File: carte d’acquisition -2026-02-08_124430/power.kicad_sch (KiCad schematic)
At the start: 19 parts, among them U1 MIC5365-3.3YC5, U4 TPS55285, U5 MIC5365-3.3YC5

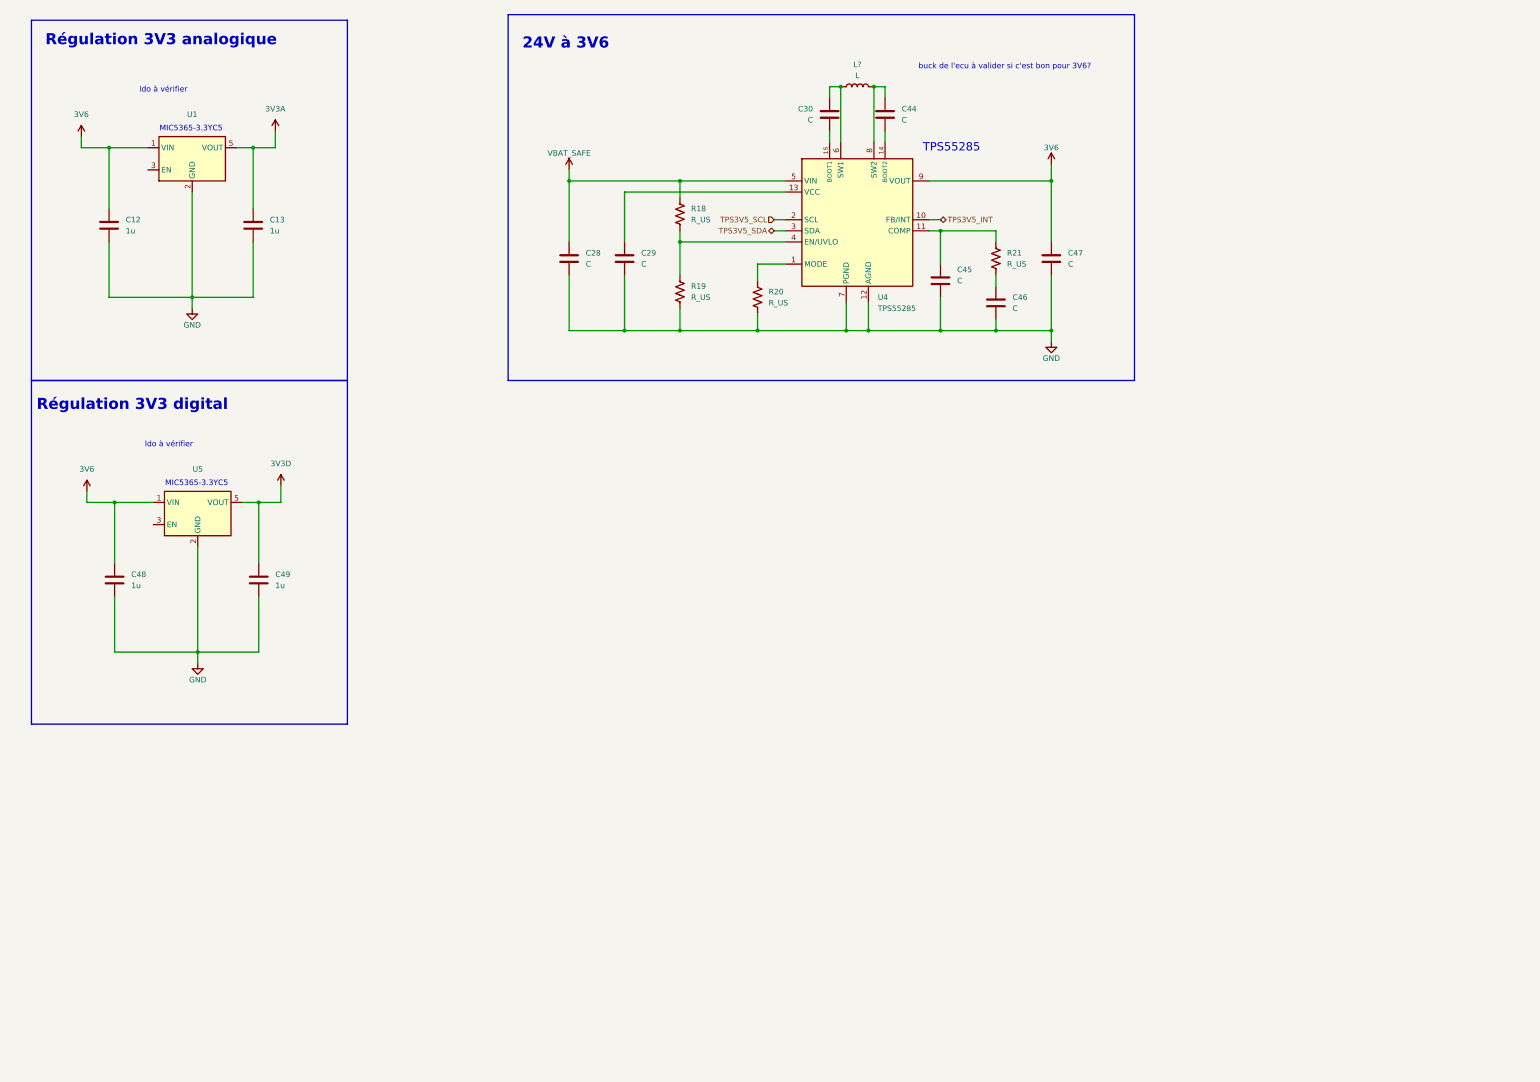
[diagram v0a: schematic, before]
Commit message: Power et maj can et sd
Modifications sur l'alim selon le schéma sur Canvas et mise à jour du can et carte sd
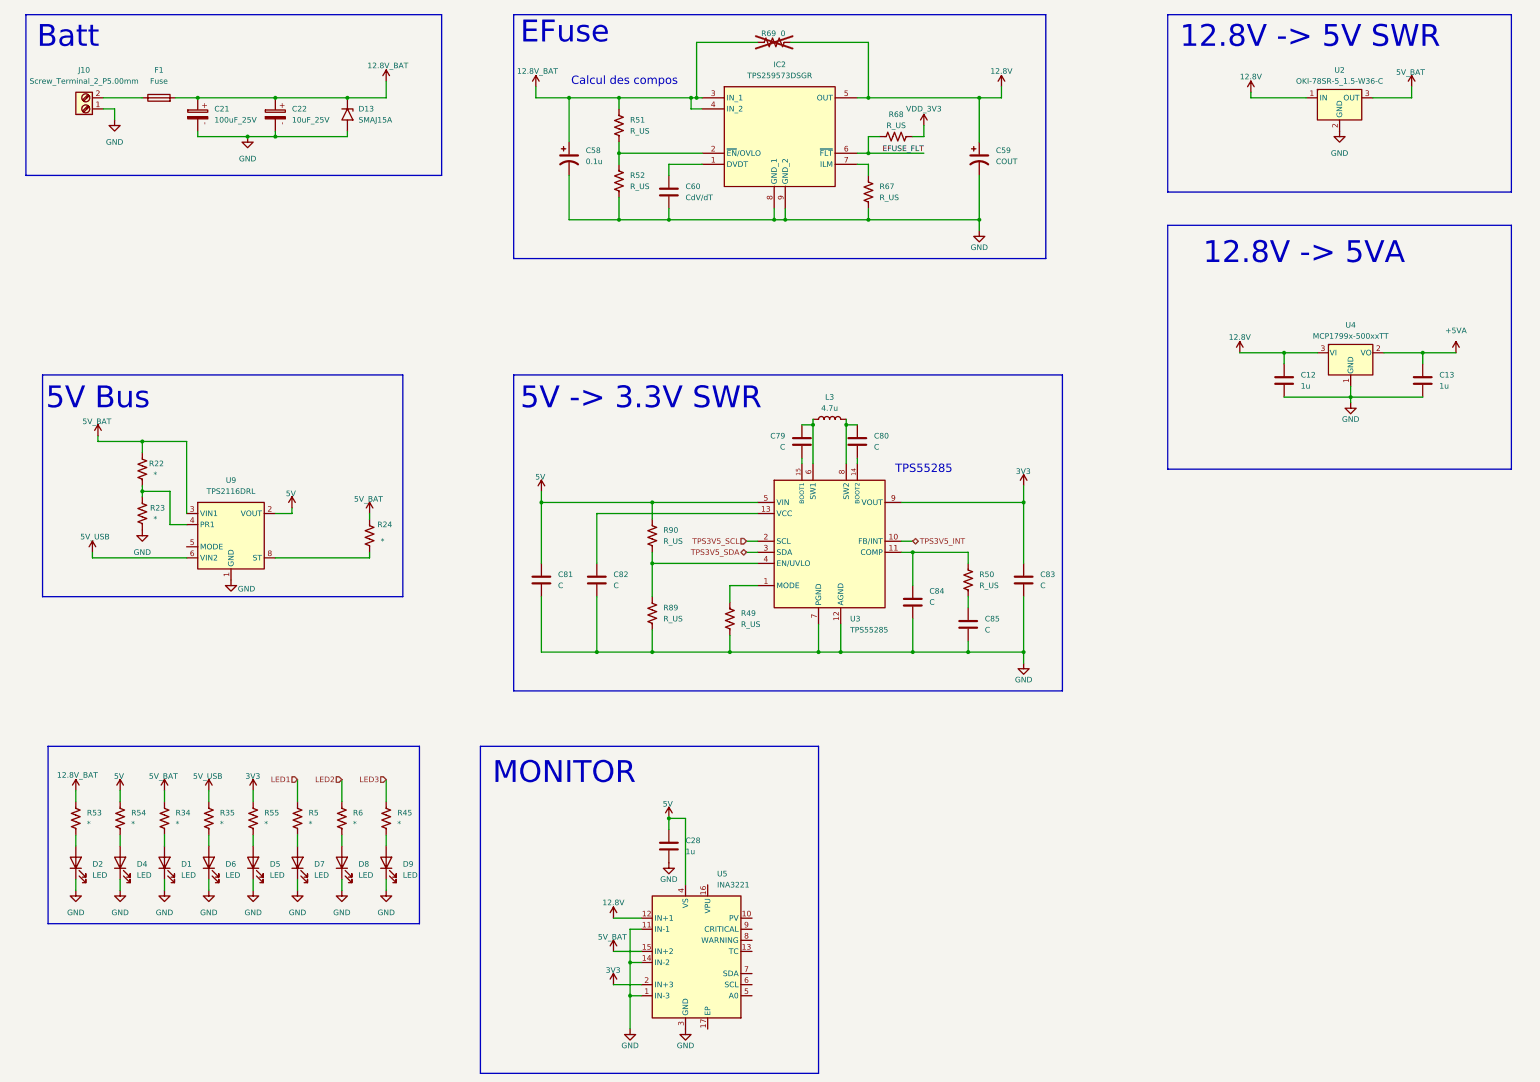
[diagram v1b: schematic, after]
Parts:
- removed C29, C30, C44, C45, C46, C47: C, symbol Device:C
- removed C48, C49: 1u, symbol Device:C
- removed L?: L, symbol Device:L
- removed R18, R19, R20, R21: R_US, symbol Device:R_US
- removed U1, U5: MIC5365-3.3YC5, Package_TO_SOT_SMD:SOT-353_SC-70-5, symbol Regulator_Linear:MIC5365-3.3YC5
- removed U4: TPS55285, symbol SiriusLib:TPS55285
- added C21: 100uF_25V, Capacitor_THT:CP_Radial_D6.3mm_P2.50mm, symbol PCM_SL_Capacitors:100uF_25V
- added C22: 10uF_25V, Capacitor_THT:CP_Radial_D5.0mm_P2.00mm, symbol PCM_SL_Capacitors:10uF_25V
- added C58: 0.1u, symbol Device:C_Polarized_US
- added C59: COUT, symbol Device:C_Polarized_US
- added C60: CdV/dT, Capacitor_SMD:C_0603_1608Metric, symbol Device:C
- added C79, C80, C81, C82, C83, C84, C85: C, Capacitor_SMD:C_0603_1608Metric, symbol Device:C
- added D1, D2, D4, D5, D6, D7, D8, D9: LED, LED_SMD:LED_0603_1608Metric, symbol Device:LED
- added D13: SMAJ15A, Diode_SMD:D_SMA, symbol Diode:SMAJ15A
- added F1: Fuse, symbol Device:Fuse
- added IC2: TPS259573DSGR, SON50P200X200X80-9N, symbol TPS259573DSGR:TPS259573DSGR
- added J10: Screw_Terminal_2_P5.00mm, TerminalBlock_Phoenix:TerminalBlock_Phoenix_PT-1,5-2-5.0-H_1x02_P5.00mm_Horizontal, symbol PCM_SL_Screw_Terminal:Screw_Terminal_2_P5.00mm
- added L3: 4.7u, symbol Device:L
- added R22, R23, R24, R53: *, Resistor_SMD:R_0805_2012Metric, symbol Device:R_US
- added R34, R35, R45, R5, R54, R55, R6: *, Resistor_SMD:R_0603_1608Metric_Pad0.98x0.95mm_HandSolder, symbol Device:R_US
- added R49, R50, R51, R52, R67, R68, R89, R90: R_US, Resistor_SMD:R_0603_1608Metric, symbol Device:R_US
- added R69: 0, Resistor_SMD:R_0603_1608Metric_Pad0.98x0.95mm_HandSolder, symbol Device:R_US
- added U2: OKI-78SR-5_1.5-W36-C, Converter_DCDC:Converter_DCDC_Murata_OKI-78SR_Vertical, symbol Converter_DCDC:OKI-78SR-5_1.5-W36-C
- added U3: TPS55285, symbol SiriusLib:TPS55285
- added U4: MCP1799x-500xxTT, Package_TO_SOT_SMD:SOT-23, symbol Regulator_Linear:MCP1799x-500xxTT
- added U5: INA3221, Package_DFN_QFN:Texas_RGV0016A_VQFN-16-1EP_4x4mm_P0.65mm_EP2.1x2.1mm, symbol Power_Management:INA3221
- added U9: TPS2116DRL, Package_TO_SOT_SMD:SOT-583-8, symbol Power_Management:TPS2116DRL
- C28: value C -> 1u
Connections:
- net GND: now also C21.2, C22.2, C58.2, C59.2, C60.2, C81.2, C82.2, C83.2, C84.2, C85.2, D1.1 (K), D13.2 (A2), D2.1 (K), D4.1 (K), D5.1 (K), D6.1 (K), D7.1 (K), D8.1 (K), D9.1 (K), IC2.8 (GND_1), IC2.9 (GND_2), J10.1, R23.1, R49.2, R52.2, R67.2, R89.2, U2.2 (GND), U3.12 (AGND), U3.7 (PGND), U4.1 (GND), U5.1 (IN-3), U5.11 (IN-1), U5.14 (IN-2), U5.3 (GND), U9.1 (GND)
- net TPS3V5_INT: now also U3.10 (FB/INT)
- net TPS3V5_SCL: now also U3.2 (SCL)
- net TPS3V5_SDA: now also U3.3 (SDA)
- net 3V3A renamed +5VA
- net +5VA: now also U4.2 (VO)
- net 3V6 renamed 12.8V
- net 12.8V: now also C59.1, IC2.5 (OUT), R69.2, U2.1 (IN), U4.3 (VI), U5.12 (IN+1)
- net VBAT_SAFE renamed 5V
- net 5V: now also C81.1, R54.2, R90.1, U3.5 (VIN), U5.4 (VS), U9.2 (VOUT), U9.7 (VOUT)
- new net: C84.1, R50.1, U3.11 (COMP)
- new net: F1.1, J10.2
- new net: C82.1, U3.13 (VCC)
- new net: D8.2 (A), R6.1
- new net: D5.2 (A), R55.1
- new net: R22.1, R23.2, U9.4 (PR1)
- new net: R24.1, U9.8 (ST)
- new net: C85.1, R50.2
- new net: D4.2 (A), R54.1
- new net: D1.2 (A), R34.1
- new net: C60.1, IC2.1 (DVDT)
- new net: IC2.2 (~{EN}/OVLO), R51.2, R52.1
- new net: IC2.7 (ILM), R67.1
- new net: D2.2 (A), R53.1
- new net: R49.1, U3.1 (MODE)
- new net: C80.2, U3.14 (BOOT2)
- new net: C79.2, U3.15 (BOOT1)
- new net: R89.1, R90.2, U3.4 (EN/UVLO)
- new net: C79.1, L3.1, U3.6 (SW1)
- new net: C80.1, L3.2, U3.8 (SW2)
- new net: D7.2 (A), R5.1
- new net: D6.2 (A), R35.1
- new net: D9.2 (A), R45.1
- new net 12.8V_BAT: C21.1, C22.1, C58.1, D13.1 (A1), F1.2, IC2.3 (IN_1), IC2.4 (IN_2), R51.1, R53.2, R69.1
- new net 3V3: C83.1, R55.2, U3.9 (VOUT), U5.2 (IN+3)
- new net 5V_BAT: R22.2, R24.2, R34.2, U2.3 (OUT), U5.15 (IN+2), U9.3 (VIN1)
- new net 5V_USB: R35.2, U9.6 (VIN2)
- new net EFUSE_FLT: IC2.6 (~{FLT}), R68.1
- new net LED1: R5.2
- new net LED2: R6.2
- new net LED3: R45.2
- new net VDD_3V3: R68.2
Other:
- note added: "12.8V -> 5V SWR"
- note added: "12.8V -> 5VA"
- note added: "5V -> 3.3V SWR"
- note added: "5V Bus"
- note added: "Batt"
- note added: "Calcul des compos"
- note added: "EFuse"
- note added: "MONITOR"
- note removed: "24V à 3V6"
- note removed: "MIC5365-3.3YC5"
- note removed: "Régulation 3V3 analogique"
- note removed: "Régulation 3V3 digital"
- note removed: "buck de l'ecu à valider si c'est bon pour 3V6?"
- note removed: "ldo à vérifier"

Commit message: Petits ajustements
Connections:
- net +5VA renamed 3V3A
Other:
- note added: "12.8V -> 3.3VA"
- note removed: "12.8V -> 5VA"
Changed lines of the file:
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@@
 		)
 	)
-	(text "12.8V -> 5VA"
+	(text "12.8V -> 3.3VA"
 		(exclude_from_sim no)
 		(at 306.832 69.85 0)
@@
 	(wire
 		(pts
-			(xy 334.01 92.71) (xy 341.63 92.71)
+			(xy 334.01 92.71) (xy 340.36 92.71)
 		)
 		(stroke
@@
 	(symbol
 		(lib_id "power:+5VA")
-		(at 341.63 92.71 0)
+		(at 340.36 92.71 0)
 		(unit 1)
 		(exclude_from_sim no)
@@
 		(on_board yes)
 		(dnp no)
-		(fields_autoplaced yes)
 		(property "Reference" "#PWR039"
-			(at 341.63 96.52 0)
+			(at 340.36 96.52 0)
 			(effects
 				(font
@@
 			)
 		)
-		(property "Value" "+5VA"
-			(at 341.63 87.63 0)
+		(property "Value" "3V3A"
+			(at 338.328 88.138 0)
 			(effects
 				(font
 					(size 1.27 1.27)
 				)
+				(justify left)
 			)
 		)
 		(property "Footprint" ""
-			(at 341.63 92.71 0)
+			(at 340.36 92.71 0)
 			(effects
 				(font
@@
 		)
 		(property "Datasheet" ""
-			(at 341.63 92.71 0)
+			(at 340.36 92.71 0)
 			(effects
 				(font
@@
 		)
 		(property "Description" "Power symbol creates a global label with name \"+5VA\""
-			(at 341.63 92.71 0)
+			(at 340.36 92.71 0)
 			(effects
 				(font

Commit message: arthur net
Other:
- note added: "je mais sa ou arthur"
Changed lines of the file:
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@@
+		)
+	)
+	(text "je mais sa ou\n\narthur"
+		(exclude_from_sim no)
+		(at 225.044 131.318 0)
+		(effects
+			(font
+				(size 1.27 1.27)
+			)
 		)
 	)

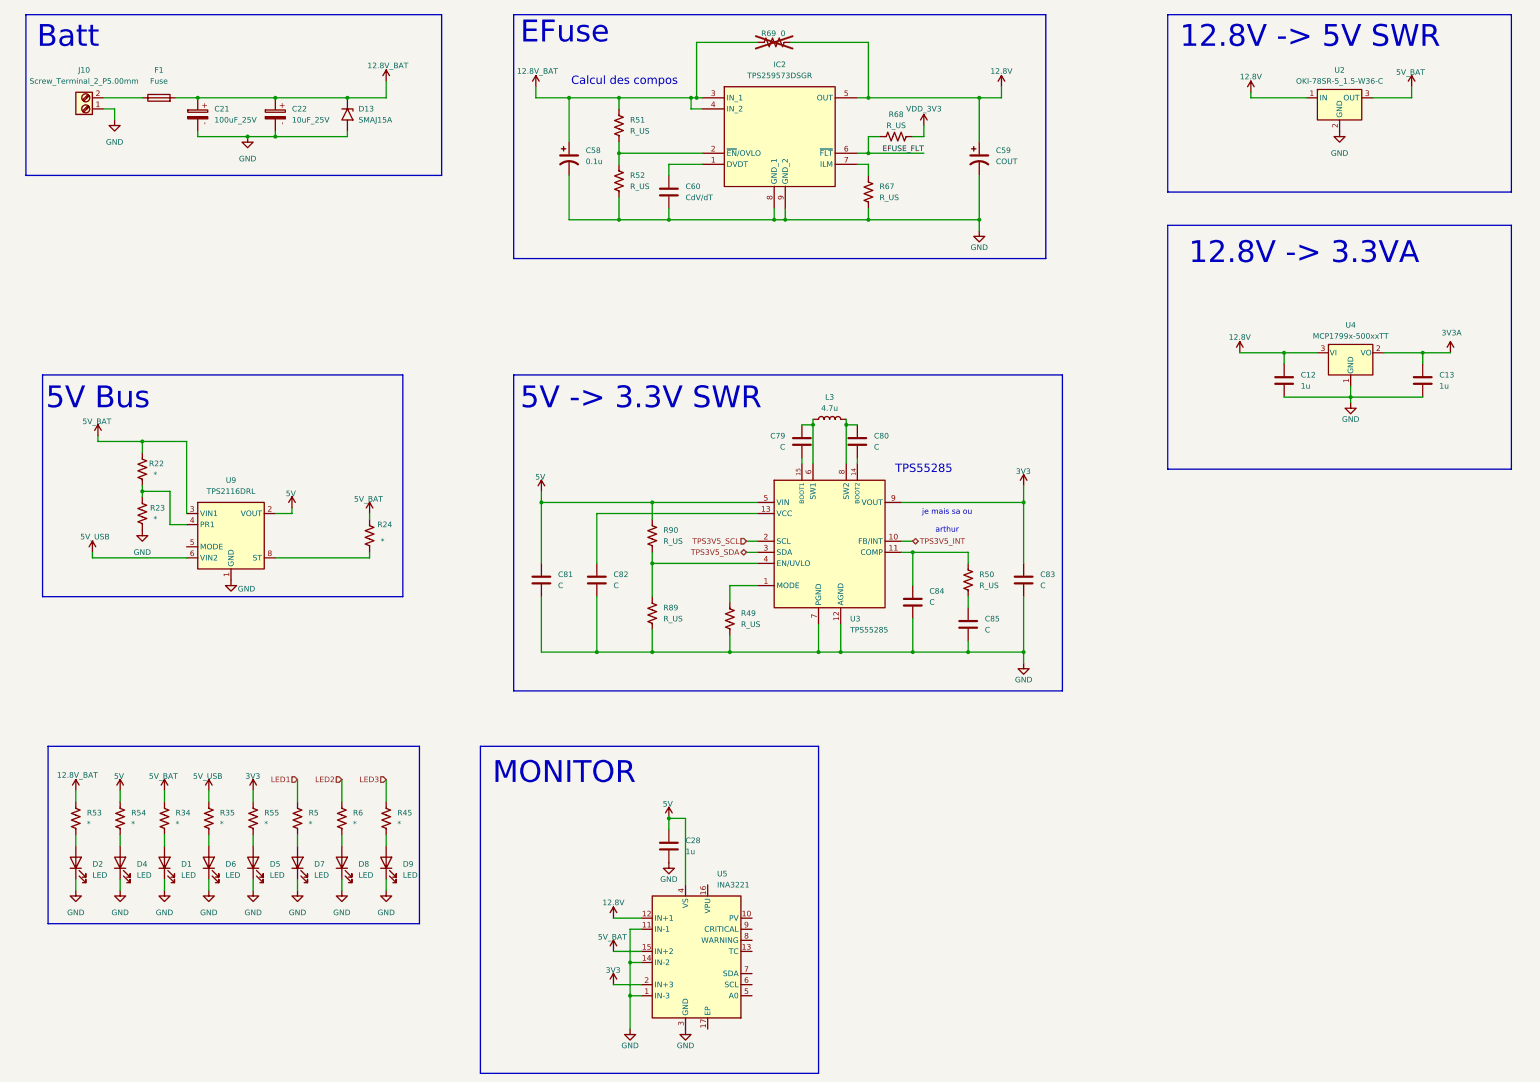
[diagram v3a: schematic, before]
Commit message: Mis a jour plusieurs circuit et ajouter beaucoup de footprint manquant
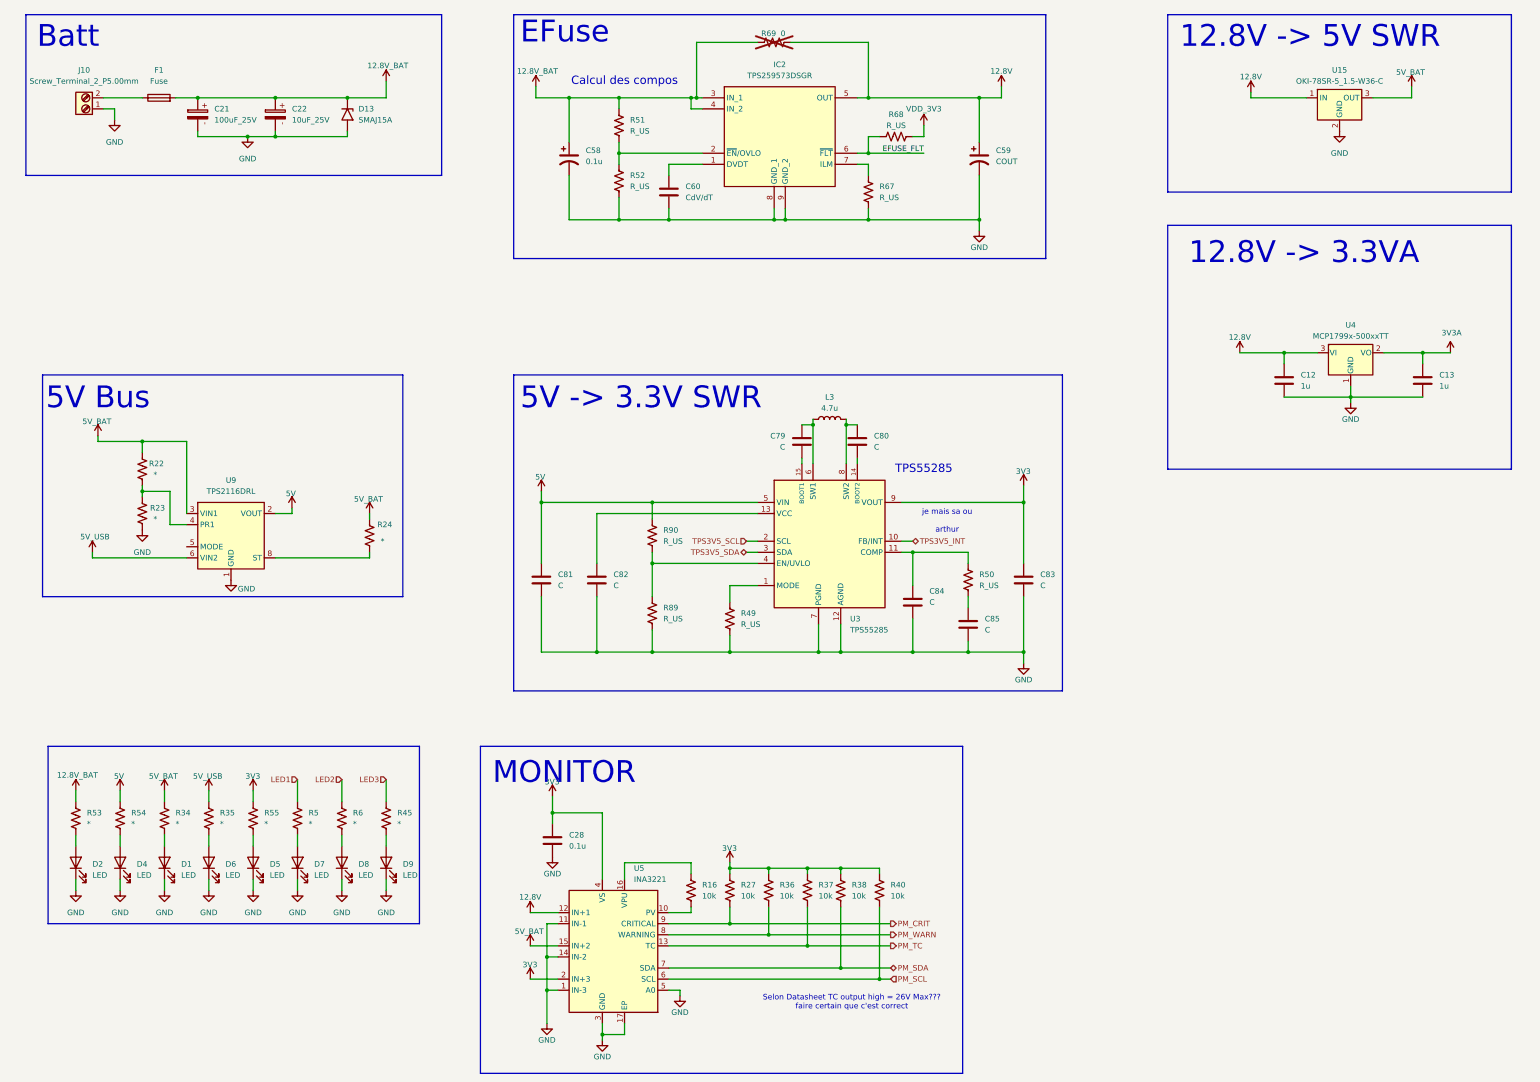
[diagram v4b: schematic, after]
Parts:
- added R16, R27, R36, R37, R38, R40: 10k, Resistor_SMD:R_0603_1608Metric_Pad0.98x0.95mm_HandSolder, symbol Device:R_US
- C12, C13: footprint (none) -> Capacitor_SMD:C_0603_1608Metric
- C28: value 1u -> 0.1u; footprint (none) -> Capacitor_SMD:C_0603_1608Metric
- F1: footprint (none) -> Fuse:Fuse_0603_1608Metric
- renumbered U2 to U15
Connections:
- net 3V3: now also C28.1, U5.4 (VS), R27.2, R36.2, R37.2, R38.2, R40.2
- net 5V: no longer C28.1, U5.4 (VS)
- net GND: now also U5.17 (EP), U5.5 (A0)
- net at U5.10 (PV): now also R16.1
- net PM_TC: now reaches U5.13 (TC)
- net PM_TC: now also R37.1
- net at U5.16 (VPU): now also R16.2
- net PM_SCL: now reaches U5.6 (SCL)
- net PM_SCL: now also R40.1
- net PM_SDA: now reaches U5.7 (SDA)
- net PM_SDA: now also R38.1
- net PM_WARN: now reaches U5.8 (WARNING)
- net PM_WARN: now also R36.1
- net PM_CRIT: now reaches U5.9 (CRITICAL)
- net PM_CRIT: now also R27.1
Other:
- note added: "Selon Datasheet TC output high = 26V Max??? faire certain que c'est correct"
- moved on the sheet: C28, U5
